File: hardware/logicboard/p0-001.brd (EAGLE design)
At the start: 91 x 57 mm, 23 parts, among them IC1 74ALS05N, IC2 LTC485N, IC3 LTC485N, J1 DIN5, J2 DIN5, J3 DIN5, X1 GLX-S-88M, X2 GLX-S-88M

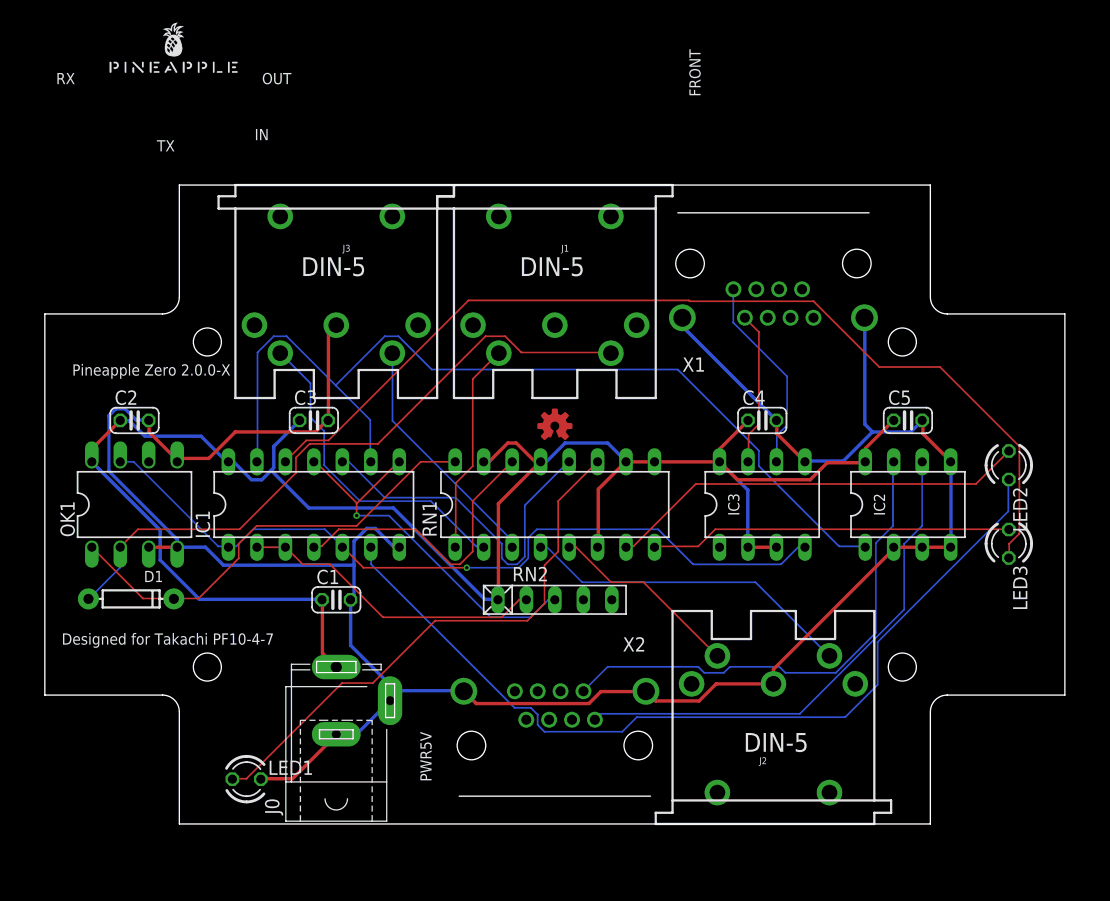
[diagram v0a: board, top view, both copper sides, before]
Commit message: Rounded corners (again).
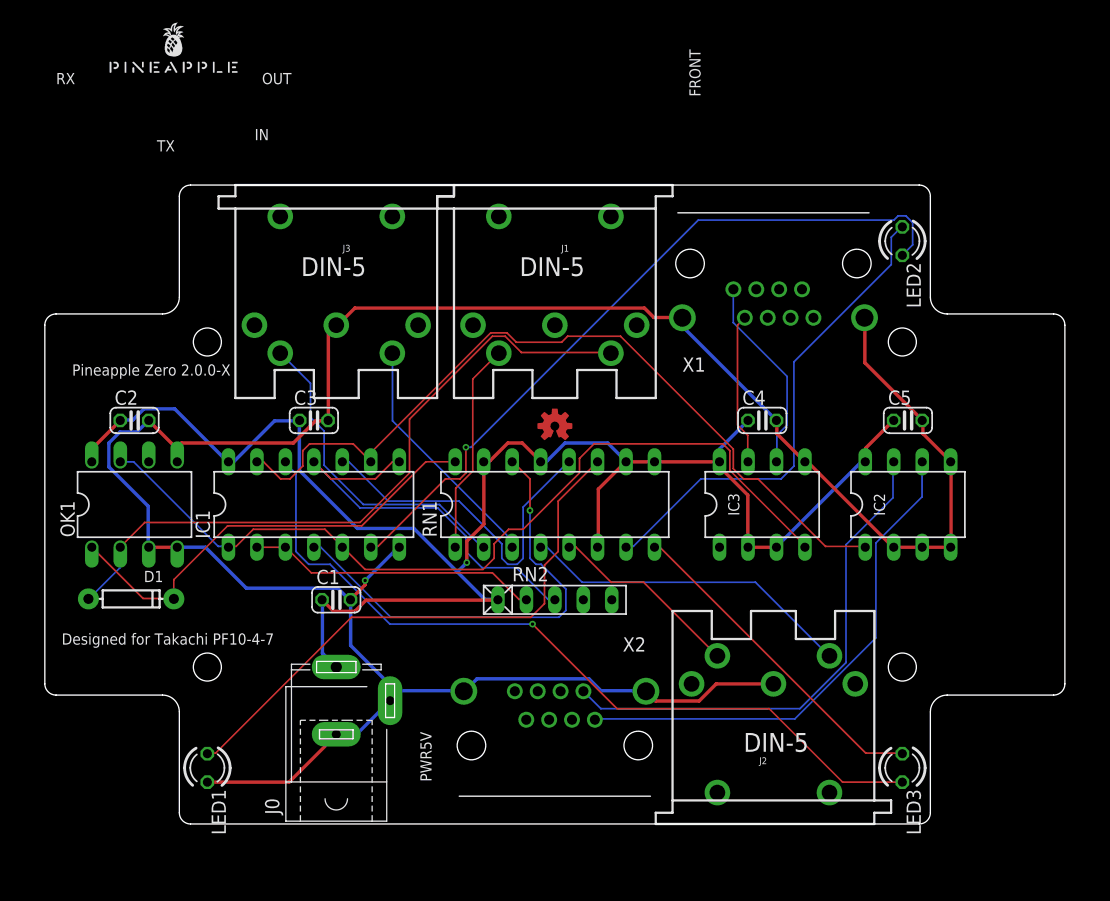
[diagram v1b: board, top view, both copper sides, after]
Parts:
- moved LED2 22.1 mm to (76.5, 52.0)
- moved LED3 22.1 mm to (76.5, 5.00)
- moved LED1 3.64 mm to (14.5, 5.00), turned to 270 degrees
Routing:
- net VCC: track 166.6 -> 149.9 mm, vias 0 -> 1
- net N$15: track 87.2 -> 71.0 mm, vias 0 -> 1
- net N$6: track 26.1 -> 40.9 mm, vias 0 -> 1
- net GND: track 212.6 -> 226.7 mm, vias 0 -> 1
- net N$2: track 78.4 -> 65.5 mm, vias 0 -> 1
- net MIDIOUT: track 84.9 -> 72.6 mm
- net N$3: track 70.8 -> 77.5 mm, vias 1 -> 0
- net N$13: track 37.7 -> 43.4 mm
- net N$14: track 32.3 -> 29.7 mm
- net N$11: track 33.9 -> 36.3 mm, vias 1 -> 0
- net MIDIIN-: track 58.8 -> 60.8 mm
- net N$5: track 27.3 -> 26.0 mm
- net N$12: track 48.9 -> 50.2 mm
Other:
- outline, holes or cut-outs redrawn

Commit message: Silk.
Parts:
- moved U$1 84.7 mm to (87.0, 28.5), turned to 90 degrees
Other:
- board text added: "4-M2.3"
- board text added: "DC5V"
- board text added: "IN/RX"
- board text added: "MIDI-IN"
- board text added: "MIDI-OUT"
- board text added: "MIDI-THRU"
- board text added: "TX/OUT"
- board text removed: "IN"
- board text removed: "PWR5V"
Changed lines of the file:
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@@
 <hole x="14.5" y="14" drill="2.5"/>
 <text x="22" y="66" size="1" layer="25" align="bottom-right">OUT</text>
-<text x="20" y="62" size="1" layer="25" align="top-right">IN</text>
 <text x="1" y="66" size="1" layer="25">RX</text>
-<text x="10" y="61" size="1" layer="25" align="top-left">TX</text>
-<text x="34" y="6" size="1" layer="25" rot="R90" align="center">PWR5V</text>
+<text x="36" y="2" size="1" layer="25" align="center">TX</text>
 <text x="58" y="67" size="1" layer="25" rot="R90" align="center">FRONT</text>
 <rectangle x1="12" y1="56" x2="79" y2="57" layer="42"/>
@@
 <rectangle x1="12" y1="0" x2="79" y2="1" layer="42"/>
 <rectangle x1="0" y1="11.5" x2="1" y2="45.5" layer="42"/>
-<text x="9.5" y="40.5" size="1" layer="25" align="center">Pineapple Zero 2.0.0-X</text>
+<text x="88" y="28.5" size="1" layer="25" rot="R90" align="center">Pineapple Zero 2.0.0-X</text>
 <hole x="76.5" y="14" drill="2.5"/>
 <hole x="76.5" y="43" drill="2.5"/>
@@
 <circle x="76.5" y="14" radius="2" width="0.2" layer="41"/>
 <circle x="76.5" y="43" radius="2" width="0.2" layer="41"/>
-<text x="1.5" y="16.5" size="1" layer="25" align="center-left">Designed for Takachi PF10-4-7</text>
+<text x="1" y="17" size="1" layer="25" align="center-left">Designed for Takachi PF10-4-7</text>
 <circle x="38" y="7" radius="2" width="0.2" layer="42"/>
 <circle x="53" y="7" radius="2" width="0.2" layer="42"/>
@@
 <circle x="38" y="7" radius="2" width="0.2" layer="41"/>
 <circle x="53" y="7" radius="2" width="0.2" layer="41"/>
+<text x="19" y="2" size="1" layer="25" align="center">DC5V</text>
+<text x="51" y="59" size="1" layer="25" align="center">MIDI-IN</text>
+<text x="19.5" y="59" size="1" layer="25" align="center">MIDI-THRU</text>
+<text x="72" y="-2" size="1" layer="25" align="center">MIDI-OUT</text>
+<text x="67.5" y="59.5" size="1" layer="25" align="center">RX</text>
+<text x="84" y="43" size="2" layer="25" align="center">IN/RX</text>
+<text x="84" y="14" size="2" layer="25" align="center">TX/OUT</text>
+<text x="10" y="14" size="1" layer="25" align="center">4-M2.3</text>
 </plain>
 <attributes>
@@
 <elements>
 <element name="D1" library="SparkFun-DiscreteSemi" library_urn="urn:adsk.eagle:library:514" package="DIODE-1N4148" package3d_urn="urn:adsk.eagle:package:38452/1" value="" x="7.7" y="20.08" smashed="yes">
-<attribute name="NAME" x="9.7" y="22.08" size="1" layer="25" ratio="10" align="center"/>
+<attribute name="NAME" x="7.7" y="21.58" size="1" layer="25" ratio="10" align="center"/>
 <attribute name="PROD_ID" value="DIO-08378" x="7.7" y="20.08" size="1.778" layer="27" display="off"/>
 <attribute name="VALUE" value="200mA/100V/1V" x="6.176" y="17.667" size="1.27" layer="27" ratio="10"/>
@@
 </element>
 <element name="LOGO1" library="SparkFun-Aesthetics" package="OSHW-LOGO-S_COPPER" value="OSHW-LOGOS-COPPER" x="45.5" y="35.5" smashed="yes"/>
-<element name="U$1" library="pineapple" package="PINEAPPLE450" value="PINEAPPLE450" x="11.5" y="67" smashed="yes"/>
+<element name="U$1" library="pineapple" package="PINEAPPLE450" value="PINEAPPLE450" x="87" y="28.5" smashed="yes" rot="R90"/>
 <element name="X1" library="con-kycon" library_urn="urn:adsk.eagle:library:157" package="GLX-S-88M" package3d_urn="urn:adsk.eagle:package:7680/1" value="GLX-S-88M" x="65" y="50" smashed="yes">
 <attribute name="MF" value="" x="65" y="50" size="1.778" layer="27" display="off"/>
@@
 <attribute name="MF" value="" x="45.5" y="7" size="1.778" layer="27" rot="R180" display="off"/>
 <attribute name="MPN" value="" x="45.5" y="7" size="1.778" layer="27" rot="R180" display="off"/>
-<attribute name="NAME" x="53.628" y="16.652" size="1.27" layer="25" rot="R180"/>
+<attribute name="NAME" x="44.628" y="-2.848" size="1.27" layer="25" rot="R180"/>
 <attribute name="OC_FARNELL" value="unknown" x="45.5" y="7" size="1.778" layer="27" rot="R180" display="off"/>
 <attribute name="OC_NEWARK" value="unknown" x="45.5" y="7" size="1.778" layer="27" rot="R180" display="off"/>
@@
 </element>
 <element name="J1" library="SparkFun-Connectors" library_urn="urn:adsk.eagle:library:513" package="DIN5-RA-PTH" package3d_urn="urn:adsk.eagle:package:38294/1" value="DIN5" x="45.5" y="57" smashed="yes" rot="R180">
-<attribute name="NAME" x="46.77" y="51.666" size="0.6096" layer="25" font="vector" ratio="20" rot="R180"/>
+<attribute name="NAME" x="38.77" y="59.166" size="0.6096" layer="25" font="vector" ratio="20" rot="R180"/>
 <attribute name="PROD_ID" value="CONN-09481" x="45.5" y="57" size="1.778" layer="27" rot="R180" display="off"/>
 <attribute name="VALUE" x="46.77" y="53.063" size="0.6096" layer="27" font="vector" ratio="20" rot="R180"/>
 </element>
 <element name="J2" library="SparkFun-Connectors" library_urn="urn:adsk.eagle:library:513" package="DIN5-RA-PTH" package3d_urn="urn:adsk.eagle:package:38294/1" value="DIN5" x="65" y="0" smashed="yes">
-<attribute name="NAME" x="63.73" y="5.334" size="0.6096" layer="25" font="vector" ratio="20"/>
+<attribute name="NAME" x="56.73" y="-4.166" size="0.6096" layer="25" font="vector" ratio="20"/>
 <attribute name="PROD_ID" value="CONN-09481" x="65" y="0" size="1.778" layer="27" display="off"/>
 <attribute name="VALUE" x="63.73" y="3.937" size="0.6096" layer="27" font="vector" ratio="20"/>
@@
 <attribute name="MF" value="" x="26" y="11" size="1.778" layer="27" rot="R90" display="off"/>
 <attribute name="MPN" value="" x="26" y="11" size="1.778" layer="27" rot="R90" display="off"/>
-<attribute name="NAME" x="20.92" y="0.84" size="1.27" layer="25" rot="R90"/>
+<attribute name="NAME" x="19.92" y="6.84" size="1.27" layer="25" rot="R90"/>
 <attribute name="OC_FARNELL" value="unknown" x="26" y="11" size="1.778" layer="27" rot="R90" display="off"/>
 <attribute name="OC_NEWARK" value="unknown" x="26" y="11" size="1.778" layer="27" rot="R90" display="off"/>
@@
 </element>
 <element name="J3" library="SparkFun-Connectors" library_urn="urn:adsk.eagle:library:513" package="DIN5-RA-PTH" package3d_urn="urn:adsk.eagle:package:38294/1" value="DIN5" x="26" y="57" smashed="yes" rot="R180">
-<attribute name="NAME" x="27.27" y="51.666" size="0.6096" layer="25" font="vector" ratio="20" rot="R180"/>
+<attribute name="NAME" x="33.27" y="60.166" size="0.6096" layer="25" font="vector" ratio="20" rot="R180"/>
 <attribute name="PROD_ID" value="CONN-09481" x="26" y="57" size="1.778" layer="27" rot="R180" display="off"/>
 <attribute name="VALUE" x="27.27" y="53.063" size="0.6096" layer="27" font="vector" ratio="20" rot="R180"/>
@@
 </element>
 <element name="LED1" library="led" library_urn="urn:adsk.eagle:library:259" package="LED3MM" package3d_urn="urn:adsk.eagle:package:15797/1" value="" x="14.5" y="5" smashed="yes" rot="R270">
-<attribute name="NAME" x="14.881" y="3.095" size="1.27" layer="25" ratio="10" rot="R270"/>
+<attribute name="NAME" x="7.381" y="3.595" size="1.27" layer="25" ratio="10" rot="R270"/>
 <attribute name="POPULARITY" value="97" x="14.5" y="5" size="1.778" layer="27" rot="R270" display="off"/>
 <attribute name="VALUE" x="12.849" y="3.095" size="1.27" layer="27" ratio="10" rot="R270"/>
 </element>
 <element name="LED2" library="led" library_urn="urn:adsk.eagle:library:259" package="LED3MM" package3d_urn="urn:adsk.eagle:package:15797/1" value="" x="76.5" y="52" smashed="yes" rot="R270">
-<attribute name="NAME" x="76.881" y="50.095" size="1.27" layer="25" ratio="10" rot="R270"/>
+<attribute name="NAME" x="86.381" y="52.095" size="1.27" layer="25" ratio="10" rot="R270"/>
 <attribute name="POPULARITY" value="97" x="76.5" y="52" size="1.778" layer="27" rot="R270" display="off"/>
 <attribute name="VALUE" x="74.849" y="50.095" size="1.27" layer="27" ratio="10" rot="R270"/>
 </element>
 <element name="LED3" library="led" library_urn="urn:adsk.eagle:library:259" package="LED3MM" package3d_urn="urn:adsk.eagle:package:15797/1" value="" x="76.5" y="5" smashed="yes" rot="R270">
-<attribute name="NAME" x="76.881" y="3.095" size="1.27" layer="25" ratio="10" rot="R270"/>
+<attribute name="NAME" x="82.881" y="2.095" size="1.27" layer="25" ratio="10" rot="R270"/>
 <attribute name="POPULARITY" value="97" x="76.5" y="5" size="1.778" layer="27" rot="R270" display="off"/>
 <attribute name="VALUE" x="74.849" y="3.095" size="1.27" layer="27" ratio="10" rot="R270"/>

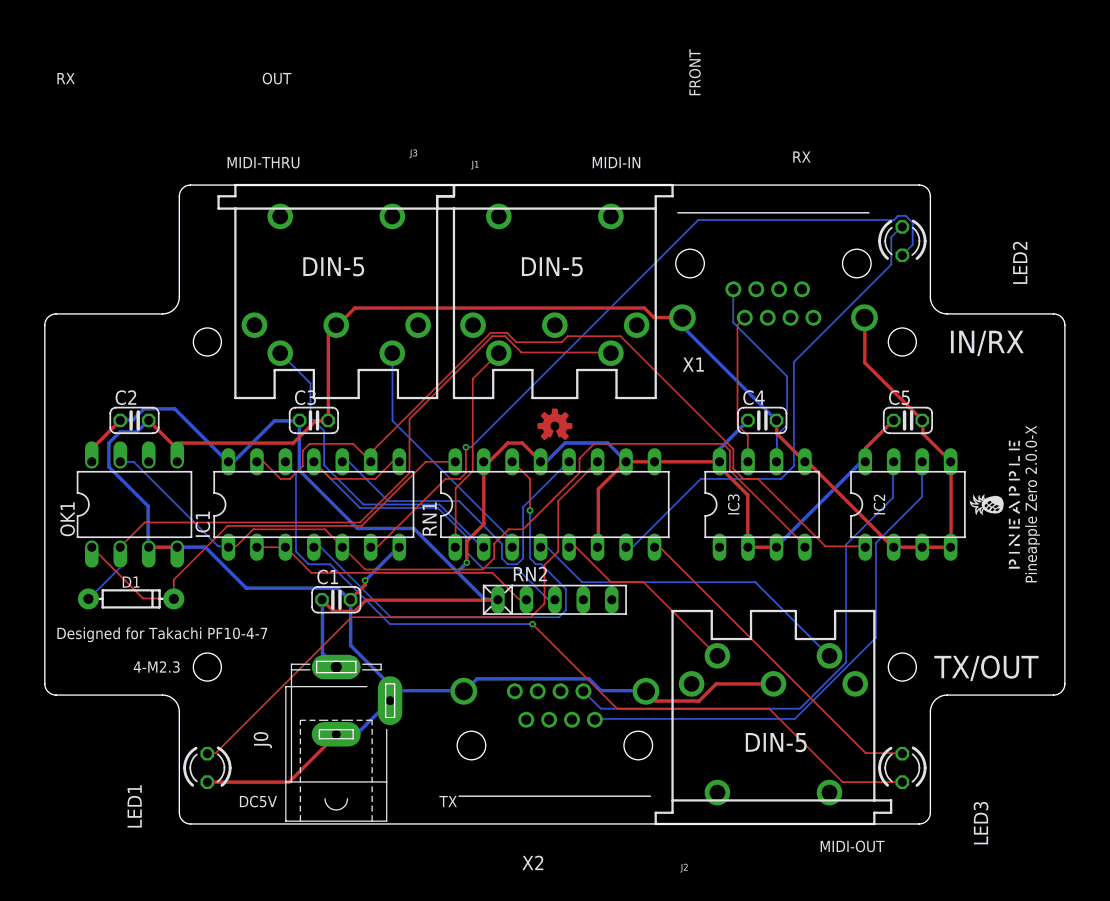
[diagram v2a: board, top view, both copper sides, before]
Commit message: Now use Neltron's RJ-45 Jack.
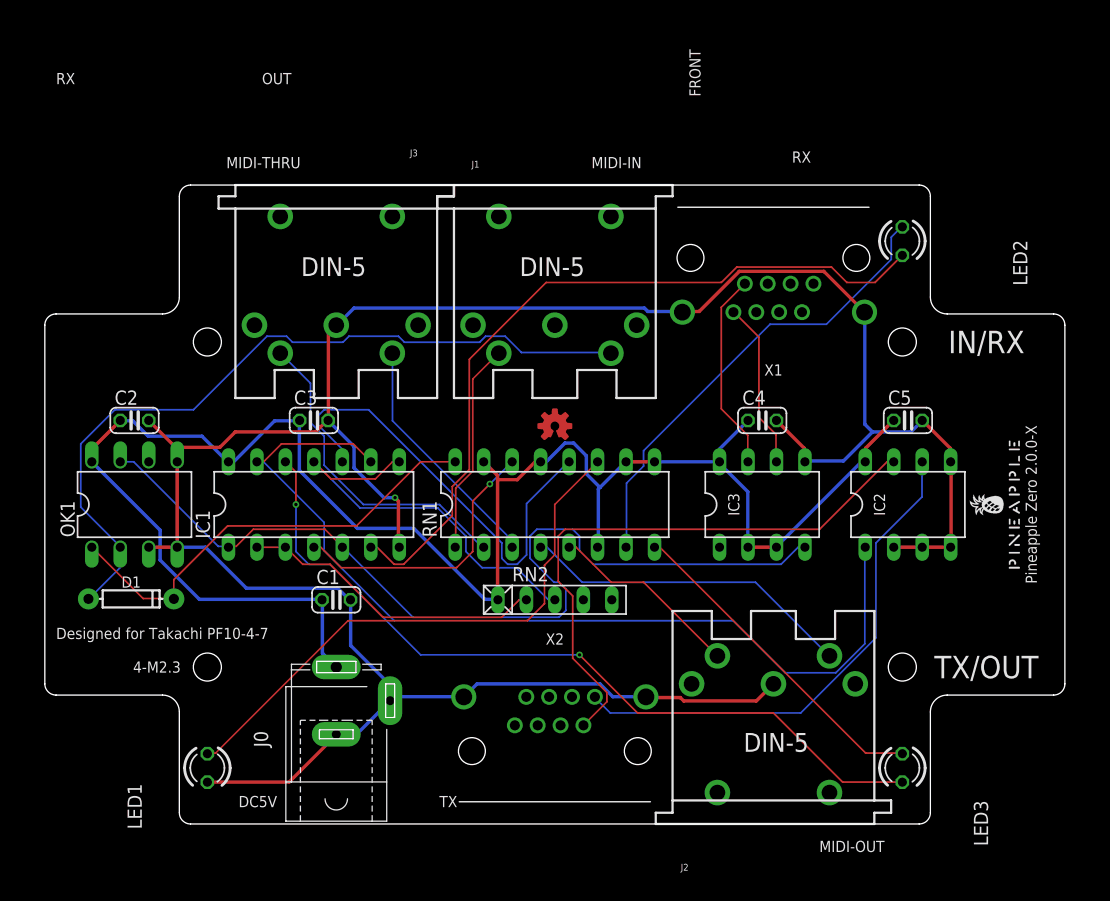
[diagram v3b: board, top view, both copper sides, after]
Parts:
- X1, X2: value GLX-S-88M -> NELTRON-7810-XPXC; device con-kycon:GLX-S-88M -> con-rj45:NELTRON-7810-XPXC-FOOTPRINT
- moved X1 0.50 mm to (65.0, 50.5)
- moved X2 0.50 mm to (45.5, 6.50)
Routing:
- net N$6: track 40.9 -> 25.0 mm
- net MIDIOUT: track 72.6 -> 84.7 mm
- net N$10: track 31.2 -> 40.7 mm
- net VCC: track 149.9 -> 159.2 mm, vias 1 -> 0
- net MIDIIN-: track 60.8 -> 69.3 mm
- net GND: track 226.7 -> 233.6 mm
- net RX-: track 45.5 -> 52.2 mm
- net N$3: track 77.5 -> 82.8 mm
- net TX-: track 13.5 -> 17.7 mm
- net TX+: track 17.8 -> 15.0 mm
- net N$2: track 65.5 -> 67.9 mm, vias 1 -> 0
- net N$13: track 43.4 -> 41.8 mm
- net N$5: track 26.0 -> 27.3 mm
- net N$15: vias 1 -> 2

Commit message: Silk.
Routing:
- net N$6: track 25.0 -> 49.3 mm, vias 1 -> 0
- net N$15: track 71.0 -> 94.3 mm, vias 2 -> 1
- net GND: track 233.6 -> 214.2 mm
- net VCC: track 159.2 -> 172.2 mm
- net N$10: track 40.7 -> 31.2 mm
- net N$3: track 82.8 -> 76.9 mm, vias 0 -> 1
- net N$2: track 67.9 -> 64.7 mm
- net MIDIIN-: track 69.3 -> 70.4 mm
- net N$11: track 36.3 -> 35.5 mm
- net MIDIOUT: track 84.7 -> 84.0 mm
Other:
- board text added: "Designed for Neltron 7810-8P8C"
- board text added: "IN"
- board text added: "MIDI IN"
- board text added: "MIDI OUT"
- board text added: "NI"
- board text added: "THRU"
- board text added: "TX/THRU"
- board text removed: "FRONT"
- board text removed: "IN/RX"
- board text removed: "MIDI-IN"
- board text removed: "MIDI-OUT"
- board text removed: "MIDI-THRU"
- board text removed: "TX/OUT"

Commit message: Routed.
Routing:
- net N$6: track 49.3 -> 28.3 mm, vias 0 -> 1
- net GND: track 214.2 -> 231.9 mm
- net VCC: track 172.2 -> 157.1 mm, vias 0 -> 1
- net MIDIIN-: track 70.4 -> 58.0 mm
- net N$3: track 76.9 -> 70.8 mm
- net N$2: track 64.7 -> 61.9 mm
- net MIDIOUT: track 84.0 -> 86.4 mm
- net RX-: track 52.2 -> 50.4 mm
- net N$5: track 27.5 -> 26.0 mm
- net TX-: track 17.7 -> 16.5 mm
- net N$11: track 35.5 -> 36.1 mm
